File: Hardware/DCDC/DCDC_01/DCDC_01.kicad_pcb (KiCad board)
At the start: 2 copper layers, 119 parts, among them Q10 Q_NMOS_GDS, Q11 Q_NMOS_GDS, Q12 Q_NMOS_GDS, Q13 Q_NMOS_GDS, Q3 Q_NMOS_GDS, Q6 Q_NMOS_GDS, Q7 Q_NMOS_GDS, Q8 Q_NMOS_GDS, Q9 Q_NMOS_GDS, SW1 PTS645SM43SMTR92 LFS, U1 PIC33EPxxxMU810, U10 OPA320-Q1, U3 LTC7810, U4 FT230X, U5 TCAN1051GVDRQ1, Y1 8MHz

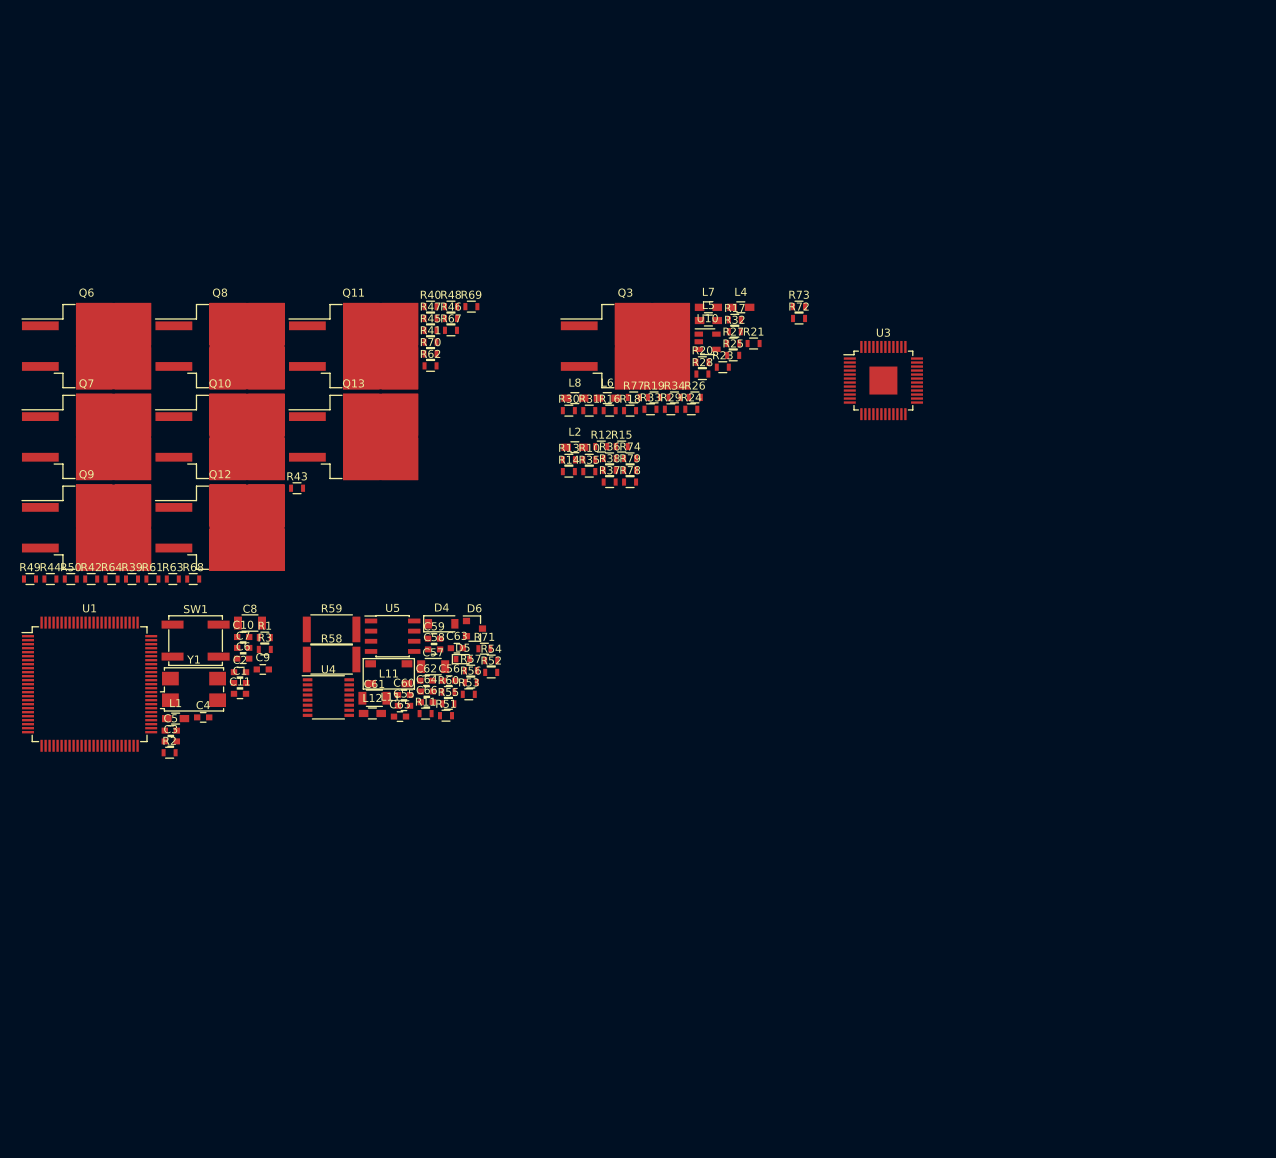
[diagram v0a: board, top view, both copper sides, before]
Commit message: Updated DCDC schematic with footprints. Moving onto BMS as higher priority. Footprints added, 5V regulator updated
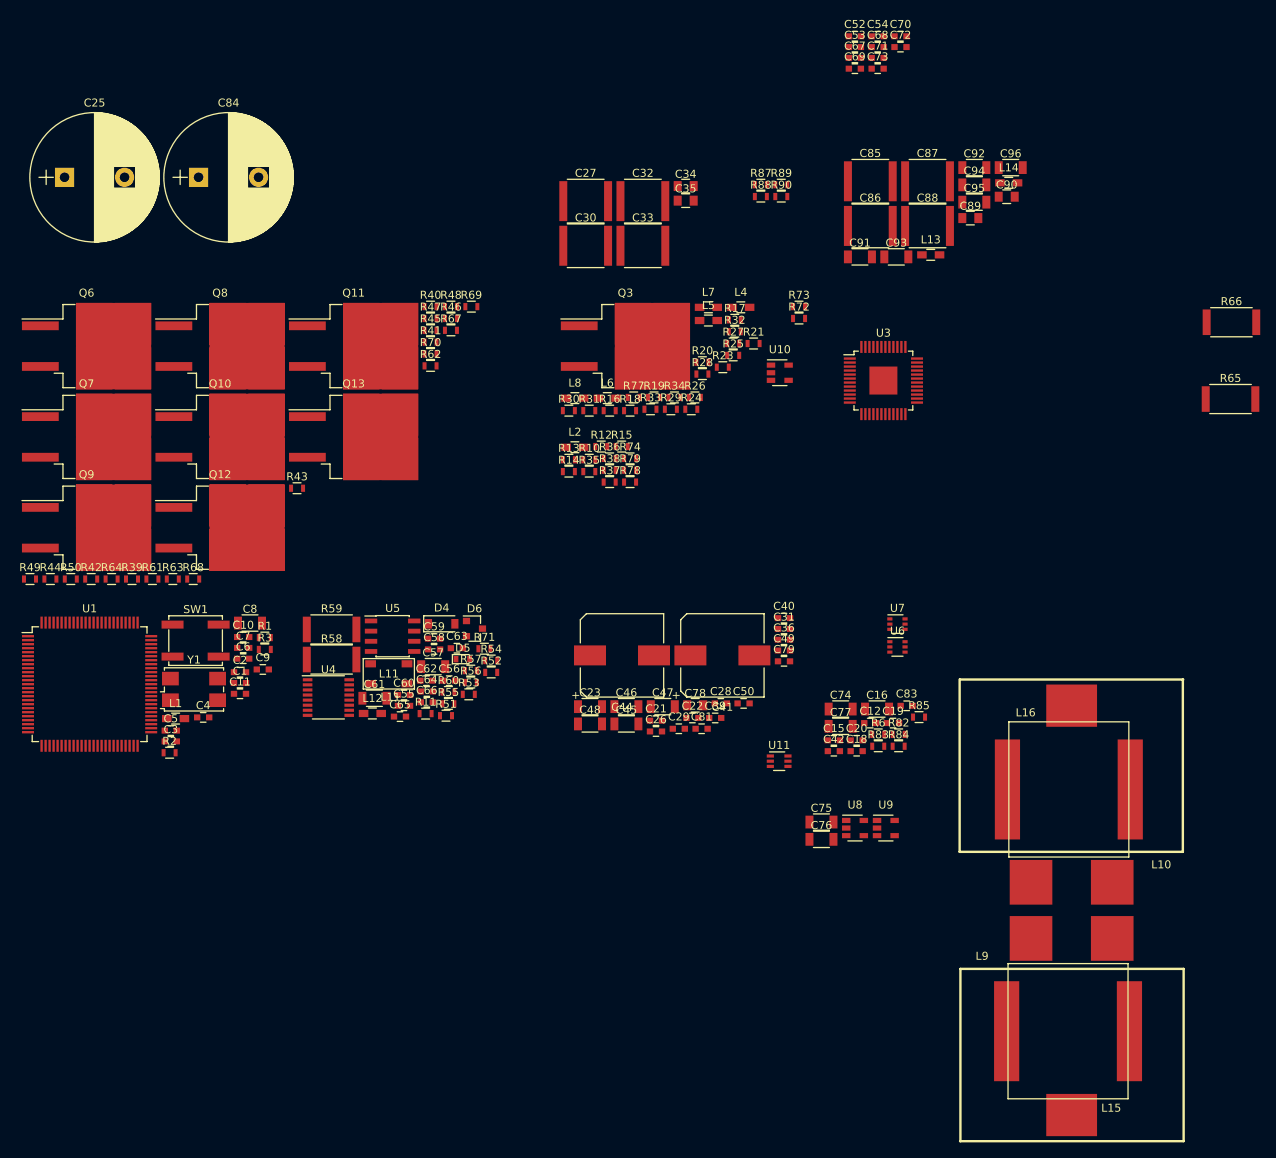
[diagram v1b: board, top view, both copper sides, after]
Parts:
- added C12: 500nF, Capacitors_SMD:C_0603, F.Cu at (256.3, 77.8)
- added C15: 330pF, Capacitors_SMD:C_0603, F.Cu at (251.8, 80.0)
- added C16: 10uF, Capacitors_SMD:C_1206, F.Cu at (257.2, 76.0)
- added C18: 100nF, Capacitors_SMD:C_0603, F.Cu at (254.6, 81.3)
- added C19: 10nF, Capacitors_SMD:C_0603, F.Cu at (259.2, 77.8)
- added C20: 100nF, Capacitors_SMD:C_0603, F.Cu at (254.6, 80.0)
- added C21: 100nF, Capacitors_SMD:C_0603, F.Cu at (229.5, 77.5)
- added C22: C, Capacitors_SMD:C_0603, F.Cu at (234.1, 77.2)
- added C23: 4.7uF, Capacitors_SMD:C_1206, F.Cu at (221.3, 75.7)
- added C25: 100uF, Capacitors_THT:CP_Radial_D16.0mm_P7.50mm, F.Cu at (155.6, 9.58)
- added C26: 10nF, Capacitors_SMD:C_0603, F.Cu at (229.5, 78.8)
- added C27: 1uF, Capacitors_SMD:C_2220, F.Cu at (220.7, 12.6)
- added C28: 47pF, Capacitors_SMD:C_0603, F.Cu at (237.6, 75.3)
- added C29: C, Capacitors_SMD:C_0603, F.Cu at (232.4, 78.5)
- added C30: 1uF, Capacitors_SMD:C_2220, F.Cu at (220.7, 18.1)
- added C31: 100nF, Capacitors_SMD:C_0603, F.Cu at (245.5, 66.0)
- added C32: 1uF, Capacitors_SMD:C_2220, F.Cu at (227.9, 12.6)
- added C33: 1uF, Capacitors_SMD:C_2220, F.Cu at (227.9, 18.1)
- added C34: 100nF, Capacitors_SMD:C_0805, F.Cu at (233.2, 10.7)
- added C35: 10nF, Capacitors_SMD:C_0805, F.Cu at (233.2, 12.5)
- added C36: 1nF, Capacitors_SMD:C_0603, F.Cu at (245.5, 67.4)
- added C39: 1nF, Capacitors_SMD:C_0603, F.Cu at (236.9, 77.2)
- added C40: C, Capacitors_SMD:C_0603, F.Cu at (245.5, 64.7)
- added C41: 220uF, Capacitors_SMD:CP_Elec_10x10, F.Cu at (237.8, 69.3)
- added C42: 100nF, Capacitors_SMD:C_0603, F.Cu at (251.8, 81.3)
- added C44: 220uF, Capacitors_SMD:CP_Elec_10x10, F.Cu at (225.3, 69.3)
- added C45: 10uF, Capacitors_SMD:C_1206, F.Cu at (225.8, 77.9)
- added C46: 10uF, Capacitors_SMD:C_1206, F.Cu at (225.8, 75.7)
- added C47: 10uF, Capacitors_SMD:C_1206, F.Cu at (230.4, 75.7)
- added C48: 10uF, Capacitors_SMD:C_1206, F.Cu at (221.3, 77.9)
- added C49: 100nF, Capacitors_SMD:C_0603, F.Cu at (245.5, 68.7)
- added C50: 10nF, Capacitors_SMD:C_0603, F.Cu at (240.5, 75.3)
- added C52: 1uF, Capacitors_SMD:C_0603, F.Cu at (254.4, -8.05)
- added C53: 100nF, Capacitors_SMD:C_0603, F.Cu at (254.4, -6.70)
- added C54: 100nF, Capacitors_SMD:C_0603, F.Cu at (257.2, -8.05)
- added C67: 1uF, Capacitors_SMD:C_0603, F.Cu at (254.4, -5.35)
- added C68: C, Capacitors_SMD:C_0603, F.Cu at (257.2, -6.70)
- added C69: C, Capacitors_SMD:C_0603, F.Cu at (254.4, -4.00)
- added C70: C, Capacitors_SMD:C_0603, F.Cu at (260.1, -8.05)
- added C71: C, Capacitors_SMD:C_0603, F.Cu at (257.2, -5.35)
- added C72: C, Capacitors_SMD:C_0603, F.Cu at (260.1, -6.70)
- added C73: C, Capacitors_SMD:C_0603, F.Cu at (257.2, -4.00)
- added C74: 10uF, Capacitors_SMD:C_1206, F.Cu at (252.6, 76.0)
- added C75: 10uF, Capacitors_SMD:C_1206, F.Cu at (250.2, 90.2)
- added C76: 10uF, Capacitors_SMD:C_1206, F.Cu at (250.2, 92.3)
- added C77: 10uF, Capacitors_SMD:C_1206, F.Cu at (252.6, 78.2)
- added C78: 1uF, Capacitors_SMD:C_0805, F.Cu at (234.4, 75.6)
- added C79: 100nF, Capacitors_SMD:C_0603, F.Cu at (245.5, 70.1)
- added C81: 100nF, Capacitors_SMD:C_0603, F.Cu at (235.2, 78.5)
- added C83: 100nF, Capacitors_SMD:C_0603, F.Cu at (260.9, 75.6)
- added C84: 100uF, Capacitors_THT:CP_Radial_D16.0mm_P7.50mm, F.Cu at (172.3, 9.58)
- added C85: 1uF, Capacitors_SMD:C_2220, F.Cu at (256.3, 10.1)
- added C86: 1uF, Capacitors_SMD:C_2220, F.Cu at (256.3, 15.7)
- added C87: 1uF, Capacitors_SMD:C_2220, F.Cu at (263.5, 10.1)
- added C88: 1uF, Capacitors_SMD:C_2220, F.Cu at (263.5, 15.7)
- added C89: 100nF, Capacitors_SMD:C_0805, F.Cu at (268.8, 14.7)
- added C90: 10nF, Capacitors_SMD:C_0805, F.Cu at (273.4, 12.0)
- added C91: 10uF, Capacitors_SMD:C_1206, F.Cu at (255.0, 19.5)
- added C92: 10uF, Capacitors_SMD:C_1206, F.Cu at (269.3, 8.36)
- added C93: 10uF, Capacitors_SMD:C_1206, F.Cu at (259.6, 19.5)
- added C94: 10uF, Capacitors_SMD:C_1206, F.Cu at (269.3, 10.5)
- added C95: 10uF, Capacitors_SMD:C_1206, F.Cu at (269.3, 12.7)
- added C96: 10uF, Capacitors_SMD:C_1206, F.Cu at (273.9, 8.36)
- added L10: L, Footprints:PQ2614BLA-6R8K, F.Cu at (281.5, 83.3)
- added L13: Ferrite_Bead, Inductors_SMD:L_0603_HandSoldering, F.Cu at (263.9, 19.3)
- added L14: Ferrite_Bead, Inductors_SMD:L_0603_HandSoldering, F.Cu at (273.6, 10.3)
- added L15: L, Footprints:SRP1770TA-100M, F.Cu at (281.0, 116.3)
- added L16: L, Footprints:SRP1770TA-100M, F.Cu at (281.1, 86.1)
- added L9: L, Footprints:PQ2614BLA-6R8K, F.Cu at (281.5, 119.1)
- added R6: 100R, Resistors_SMD:R_0603, F.Cu at (257.3, 79.2)
- added R65: R, Resistors_SMD:R_2512, F.Cu at (301.3, 37.3)
- added R66: R, Resistors_SMD:R_2512, F.Cu at (301.5, 27.7)
- added R82: 10k, Resistors_SMD:R_0603, F.Cu at (259.9, 79.2)
- added R83: 100k, Resistors_SMD:R_0603, F.Cu at (257.3, 80.7)
- added R84: 47k, Resistors_SMD:R_0603, F.Cu at (259.9, 80.7)
- added R85: 10k, Resistors_SMD:R_0603, F.Cu at (262.4, 77.1)
- added R87: 100k, Resistors_SMD:R_0603, F.Cu at (242.6, 10.5)
- added R88: 47k, Resistors_SMD:R_0603, F.Cu at (242.6, 12.0)
- added R89: 10k, Resistors_SMD:R_0603, F.Cu at (245.2, 10.5)
- added R90: 10k, Resistors_SMD:R_0603, F.Cu at (245.2, 12.0)
- added U11: TPL0401B-10-Q1, TO_SOT_Packages_SMD:Texas_R-PDSO-G6, F.Cu at (244.9, 82.6)
- added U6: INA21x, TO_SOT_Packages_SMD:SOT-363_SC-70-6, F.Cu at (259.7, 68.3)
- added U7: INA21x, TO_SOT_Packages_SMD:SOT-363_SC-70-6, F.Cu at (259.7, 65.4)
- added U8: TPS73633DBV, TO_SOT_Packages_SMD:SOT-23-5, F.Cu at (254.4, 90.9)
- added U9: TPS73633DBV, TO_SOT_Packages_SMD:SOT-23-5, F.Cu at (258.3, 90.9)
- moved U10 9.82 mm to (245.0, 34.0)
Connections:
- net /Top_Level/DCDC_Controller/VBATT_FILT_NDRV renamed /Top_Level/DCDC_Controller/VBATT_FILT_NDRV_HV
- net /Top_Level/DCDC_Controller/Vin renamed /Top_Level/DCDC_Controller/Vin_HV
- net /Top_Level/PowerRails/VBATT_FILT_5V renamed /Top_Level/PowerRails/VBATT_FILT_5V_HV
- net Net-(R21-Pad1) renamed /Top_Level/DCDC_Controller/12V_ULVO_HV
- net Net-(R75-Pad1) renamed /Top_Level/DCDC_Controller/12V_OLVO_HV
- L4 pad 1: VBATT_FILT -> VBATT_FILT_PHASE_2_HV
- L5 pad 1: VBATT_FILT -> VBATT_FILT_PHASE_2_HV
- Q10 pad 2: VBATT_FILT -> VBATT_FILT_PHASE_1_HV
- Q12 pad 2: VBATT_FILT -> VBATT_FILT_PHASE_2_HV
- Q6 pad 2: VBATT_FILT -> VBATT_FILT_PHASE_1_HV
- Q8 pad 2: VBATT_FILT -> VBATT_FILT_PHASE_2_HV
- R10 pad 1: Net-(C15-Pad2) -> /Top_Level/PowerRails/5V_SNUB_HV
- R13 pad 2: 12V_MONITOR_AI -> Net-(R13-Pad2)
- R14 pad 1: 12V_MONITOR_AI -> Net-(R13-Pad2)
- U1 pad 35: Net-(U1-Pad35) -> VBATT_MONITOR_AI
- U1 pad 41: Net-(U1-Pad41) -> 5V_MONITOR_AI
- U1 pad 6: 5V_MONITOR_AI -> Net-(U1-Pad6)
